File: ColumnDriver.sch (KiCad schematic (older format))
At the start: 7 parts

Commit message: Assigned footprints, add buffer capacitor, change description texts
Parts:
- added C?: 1uF, Capacitors_SMD:C_0805, symbol C_Small
- C1: renamed from C?; value C_Small -> 100nF; footprint (none) -> Capacitors_SMD:C_0603
- J1, J3: renamed from J?; footprint (none) -> Pin_Headers:Pin_Header_Straight_1x05_Pitch2.54mm
- J2: renamed from J?; footprint (none) -> Pin_Headers:Pin_Header_Straight_1x02_Pitch2.54mm
- J4: renamed from J?; footprint (none) -> Pin_Headers:Pin_Header_Straight_1x16_Pitch2.54mm
- U1: renamed from U?; value 74HC595 -> 74HCT595; footprint (none) -> Housings_SOIC:SOIC-16_3.9x9.9mm_Pitch1.27mm
- U2: renamed from U?; footprint (none) -> Housings_SOIC:SOIC-18W_7.5x11.6mm_Pitch1.27mm
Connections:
- net GND: now also U1.13 (G), C?.2
- net VCC: now also C?.1
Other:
- note added: "+5V0"
- note added: "Decoupling / Buffer"
- note added: "Inductors"
- note added: "Output"
- note removed: "+3V3 - +5V0"
- note removed: "Decoupling"
- moved on the sheet: C1
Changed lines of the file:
@@
 $EndDescr
 $Comp
-L 74HC595 U?
+L 74HC595 U1
 U 1 1 59204501
 P 4850 3200
-F 0 "U?" H 5000 3800 50  0000 C CNN
-F 1 "74HC595" H 4850 2600 50  0000 C CNN
-F 2 "" H 4850 3200 50  0001 C CNN
+F 0 "U1" H 5000 3800 50  0000 C CNN
+F 1 "74HCT595" H 4850 2600 50  0000 C CNN
+F 2 "Housings_SOIC:SOIC-16_3.9x9.9mm_Pitch1.27mm" H 4850 3200 50  0001 C CNN
 F 3 "" H 4850 3200 50  0001 C CNN
 	1    4850 3200
@@
 $EndComp
 $Comp
-L CONN_01X05 J?
+L CONN_01X05 J1
 U 1 1 59204744
 P 850 2050
-F 0 "J?" H 850 2350 50  0000 C CNN
+F 0 "J1" H 850 2350 50  0000 C CNN
 F 1 "CONN_01X05" V 950 2050 50  0000 C CNN
-F 2 "" H 850 2050 50  0001 C CNN
+F 2 "Pin_Headers:Pin_Header_Straight_1x05_Pitch2.54mm" H 850 2050 50  0001 C CNN
 F 3 "" H 850 2050 50  0001 C CNN
 	1    850  2050
@@
 $EndComp
 $Comp
-L CONN_01X05 J?
+L CONN_01X05 J3
 U 1 1 592048A3
 P 10700 1950
-F 0 "J?" H 10700 2250 50  0000 C CNN
+F 0 "J3" H 10700 2250 50  0000 C CNN
 F 1 "CONN_01X05" V 10800 1950 50  0000 C CNN
-F 2 "" H 10700 1950 50  0001 C CNN
+F 2 "Pin_Headers:Pin_Header_Straight_1x05_Pitch2.54mm" H 10700 1950 50  0001 C CNN
 F 3 "" H 10700 1950 50  0001 C CNN
 	1    10700 1950
@@
 DOUT
 $Comp
-L GND #PWR?
+L GND #PWR6
 U 1 1 59204A7B
 P 1300 1950
-F 0 "#PWR?" H 1300 1700 50  0001 C CNN
+F 0 "#PWR6" H 1300 1700 50  0001 C CNN
 F 1 "GND" H 1300 1800 50  0000 C CNN
 F 2 "" H 1300 1950 50  0001 C CNN
@@
 DOUT
 $Comp
-L VCC #PWR?
+L VCC #PWR3
 U 1 1 59204C65
 P 1150 1800
-F 0 "#PWR?" H 1150 1650 50  0001 C CNN
+F 0 "#PWR3" H 1150 1650 50  0001 C CNN
 F 1 "VCC" H 1150 1950 50  0000 C CNN
 F 2 "" H 1150 1800 50  0001 C CNN
@@
 $EndComp
 $Comp
-L GND #PWR?
+L GND #PWR2
 U 1 1 59204D53
-P 900 7450
-F 0 "#PWR?" H 900 7200 50  0001 C CNN
-F 1 "GND" H 900 7300 50  0000 C CNN
-F 2 "" H 900 7450 50  0001 C CNN
-F 3 "" H 900 7450 50  0001 C CNN
-	1    900  7450
-	1    0    0    -1
-$EndComp
-$Comp
-L VCC #PWR?
+P 1350 7450
+F 0 "#PWR2" H 1350 7200 50  0001 C CNN
+F 1 "GND" H 1350 7300 50  0000 C CNN
+F 2 "" H 1350 7450 50  0001 C CNN
+F 3 "" H 1350 7450 50  0001 C CNN
+	1    1350 7450
+	1    0    0    -1
+$EndComp
+$Comp
+L VCC #PWR1
 U 1 1 59204E34
-P 900 7050
-F 0 "#PWR?" H 900 6900 50  0001 C CNN
-F 1 "VCC" H 900 7200 50  0000 C CNN
-F 2 "" H 900 7050 50  0001 C CNN
-F 3 "" H 900 7050 50  0001 C CNN
-	1    900  7050
-	1    0    0    -1
-$EndComp
-$Comp
-L C_Small C?
+P 1350 7050
+F 0 "#PWR1" H 1350 6900 50  0001 C CNN
+F 1 "VCC" H 1350 7200 50  0000 C CNN
+F 2 "" H 1350 7050 50  0001 C CNN
+F 3 "" H 1350 7050 50  0001 C CNN
+	1    1350 7050
+	1    0    0    -1
+$EndComp
+$Comp
+L C_Small C1
 U 1 1 59204EED
-P 900 7250
-F 0 "C?" H 910 7320 50  0000 L CNN
-F 1 "C_Small" H 910 7170 50  0000 L CNN
-F 2 "" H 900 7250 50  0001 C CNN
-F 3 "" H 900 7250 50  0001 C CNN
-	1    900  7250
-	1    0    0    -1
-$EndComp
-$Comp
-L CONN_01X02 J?
+P 1350 7250
+F 0 "C1" H 1360 7320 50  0000 L CNN
+F 1 "100nF" H 1360 7170 50  0000 L CNN
+F 2 "Capacitors_SMD:C_0603" H 1350 7250 50  0001 C CNN
+F 3 "" H 1350 7250 50  0001 C CNN
+	1    1350 7250
+	1    0    0    -1
+$EndComp
+$Comp
+L CONN_01X02 J2
 U 1 1 5920547C
 P 900 850
-F 0 "J?" H 900 1000 50  0000 C CNN
+F 0 "J2" H 900 1000 50  0000 C CNN
 F 1 "CONN_01X02" V 1000 850 50  0000 C CNN
-F 2 "" H 900 850 50  0001 C CNN
+F 2 "Pin_Headers:Pin_Header_Straight_1x02_Pitch2.54mm" H 900 850 50  0001 C CNN
 F 3 "" H 900 850 50  0001 C CNN
 	1    900  850
@@
 $EndComp
 $Comp
-L GND #PWR?
+L GND #PWR5
 U 1 1 592054FB
 P 1200 950
-F 0 "#PWR?" H 1200 700 50  0001 C CNN
+F 0 "#PWR5" H 1200 700 50  0001 C CNN
 F 1 "GND" H 1200 800 50  0000 C CNN
 F 2 "" H 1200 950 50  0001 C CNN
@@
 $EndComp
 $Comp
-L VDD #PWR?
+L VDD #PWR4
 U 1 1 59205580
 P 1200 750
-F 0 "#PWR?" H 1200 600 50  0001 C CNN
+F 0 "#PWR4" H 1200 600 50  0001 C CNN
 F 1 "VDD" H 1200 900 50  0000 C CNN
 F 2 "" H 1200 750 50  0001 C CNN
@@
 	1    0    0    -1
 $EndComp
-Text Notes 550  600  0    60   ~ 0
+Text Notes 700  600  0    60   ~ 0
 +7V0
-Text Notes 550  1550 0    60   ~ 0
-+3V3 - +5V0
-$Comp
-L VDD #PWR?
+Text Notes 650  1700 0    60   ~ 0
++5V0
+$Comp
+L VDD #PWR9
 U 1 1 59205882
 P 6900 3550
-F 0 "#PWR?" H 6900 3400 50  0001 C CNN
+F 0 "#PWR9" H 6900 3400 50  0001 C CNN
 F 1 "VDD" H 6900 3700 50  0000 C CNN
 F 2 "" H 6900 3550 50  0001 C CNN
@@
 $EndComp
 $Comp
-L GND #PWR?
+L GND #PWR8
 U 1 1 592058D5
 P 6450 3850
-F 0 "#PWR?" H 6450 3600 50  0001 C CNN
+F 0 "#PWR8" H 6450 3600 50  0001 C CNN
 F 1 "GND" H 6450 3700 50  0000 C CNN
 F 2 "" H 6450 3850 50  0001 C CNN
@@
 	1    0    0    -1
 $EndComp
-Text Notes 550  1400 0    60   ~ 0
+Text Notes 650  1550 0    60   ~ 0
 Input
-Text Notes 550  6700 0    60   ~ 0
-Decoupling
-$Comp
-L CONN_01X16 J?
+Text Notes 650  6800 0    60   ~ 0
+Decoupling / Buffer
+$Comp
+L CONN_01X16 J4
 U 1 1 59205A9C
 P 10700 3400
-F 0 "J?" H 10700 4250 50  0000 C CNN
+F 0 "J4" H 10700 4250 50  0000 C CNN
 F 1 "CONN_01X16" V 10800 3400 50  0000 C CNN
-F 2 "" H 10700 3400 50  0001 C CNN
+F 2 "Pin_Headers:Pin_Header_Straight_1x16_Pitch2.54mm" H 10700 3400 50  0001 C CNN
 F 3 "" H 10700 3400 50  0001 C CNN
 	1    10700 3400
@@
 $EndComp
 $Comp
-L VDD #PWR?
+L VDD #PWR11
 U 1 1 59205AFC
 P 10350 2600
-F 0 "#PWR?" H 10350 2450 50  0001 C CNN
+F 0 "#PWR11" H 10350 2450 50  0001 C CNN
 F 1 "VDD" H 10350 2750 50  0000 C CNN
 F 2 "" H 10350 2600 50  0001 C CNN
@@
 DOT_6
 $Comp
-L ULN2803A U?
+L ULN2803A U2
 U 1 1 5920634D
 P 6450 3050
-F 0 "U?" H 6450 3575 50  0000 C CNN
+F 0 "U2" H 6450 3575 50  0000 C CNN
 F 1 "ULN2803A" H 6450 3500 50  0000 C CNN
-F 2 "" H 6500 2400 50  0001 L CNN
+F 2 "Housings_SOIC:SOIC-18W_7.5x11.6mm_Pitch1.27mm" H 6500 2400 50  0001 L CNN
 F 3 "" H 6550 2950 50  0001 C CNN
 	1    6450 3050
@@
 DOT_7
 $Comp
-L VCC #PWR?
+L VCC #PWR12
 U 1 1 59206E49
 P 10400 1700
-F 0 "#PWR?" H 10400 1550 50  0001 C CNN
+F 0 "#PWR12" H 10400 1550 50  0001 C CNN
 F 1 "VCC" H 10400 1850 50  0000 C CNN
 F 2 "" H 10400 1700 50  0001 C CNN
@@
 $EndComp
 $Comp
-L GND #PWR?
+L GND #PWR10
 U 1 1 59206E70
 P 10200 1850
-F 0 "#PWR?" H 10200 1600 50  0001 C CNN
+F 0 "#PWR10" H 10200 1600 50  0001 C CNN
 F 1 "GND" H 10200 1700 50  0000 C CNN
 F 2 "" H 10200 1850 50  0001 C CNN
@@
 	1150 1850 1150 1800
 Wire Wire Line
-	900  7150 900  7050
-Wire Wire Line
-	900  7350 900  7450
+	1350 7150 1350 7050
+Wire Wire Line
+	1350 7350 1350 7450
 Wire Wire Line
 	4150 2750 3950 2750
@@
 Wire Wire Line
 	10500 2050 10250 2050
+$Comp
+L GND #PWR7
+U 1 1 592167C3
+P 4050 3450
+F 0 "#PWR7" H 4050 3200 50  0001 C CNN
+F 1 "GND" H 4050 3300 50  0000 C CNN
+F 2 "" H 4050 3450 50  0001 C CNN
+F 3 "" H 4050 3450 50  0001 C CNN
+	1    4050 3450
+	1    0    0    -1
+$EndComp
+Wire Wire Line
+	4150 3350 4050 3350
+Wire Wire Line
+	4050 3350 4050 3450
+Text Notes 10300 2400 0    60   ~ 0
+Inductors
+Text Notes 10350 1500 0    60   ~ 0
+Output
+$Comp
+L C_Small C?
+U 1 1 59216FCE
+P 900 7250
+F 0 "C?" H 910 7320 50  0000 L CNN
+F 1 "1uF" H 910 7170 50  0000 L CNN
+F 2 "Capacitors_SMD:C_0805" H 900 7250 50  0001 C CNN
+F 3 "" H 900 7250 50  0001 C CNN
+	1    900  7250
+	1    0    0    -1
+$EndComp
+$Comp
+L VCC #PWR?
+U 1 1 5921706D
+P 900 7050
+F 0 "#PWR?" H 900 6900 50  0001 C CNN
+F 1 "VCC" H 900 7200 50  0000 C CNN
+F 2 "" H 900 7050 50  0001 C CNN
+F 3 "" H 900 7050 50  0001 C CNN
+	1    900  7050
+	1    0    0    -1
+$EndComp
+$Comp
+L GND #PWR?
+U 1 1 59217090
+P 900 7450
+F 0 "#PWR?" H 900 7200 50  0001 C CNN
+F 1 "GND" H 900 7300 50  0000 C CNN
+F 2 "" H 900 7450 50  0001 C CNN
+F 3 "" H 900 7450 50  0001 C CNN
+	1    900  7450
+	1    0    0    -1
+$EndComp
+Wire Wire Line
+	900  7050 900  7150
+Wire Wire Line
+	900  7350 900  7450
 $EndSCHEMATC

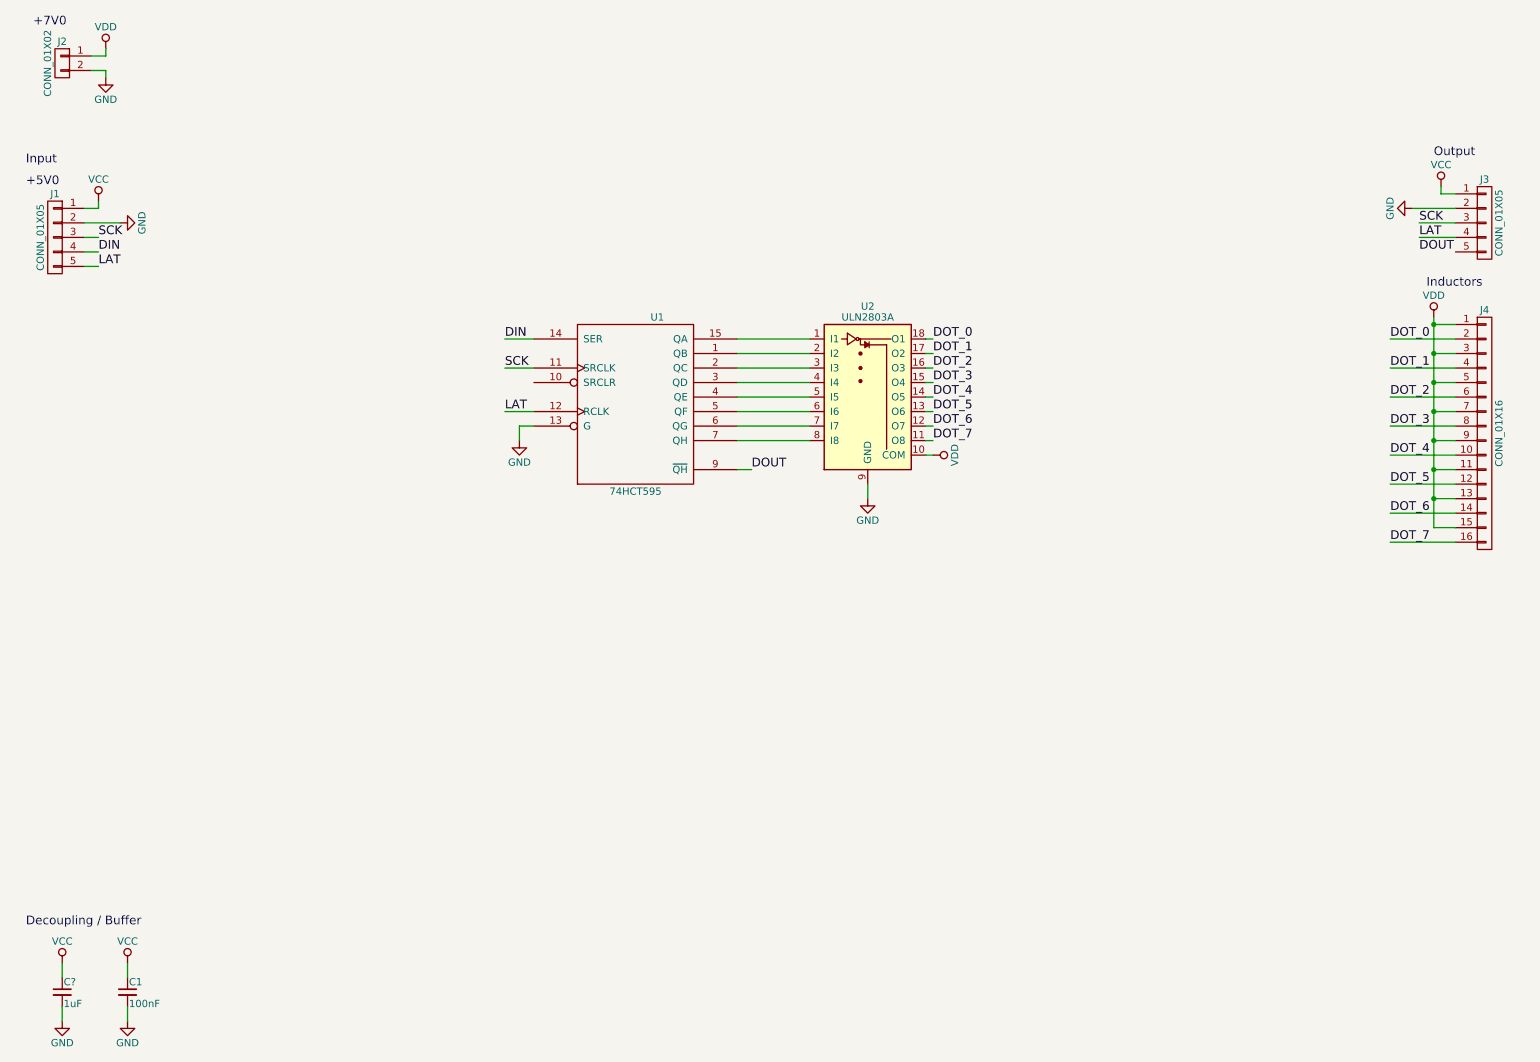
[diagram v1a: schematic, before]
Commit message: First Layout, incl. schematic adaption, 16x smd pads instead of one connector 1x16
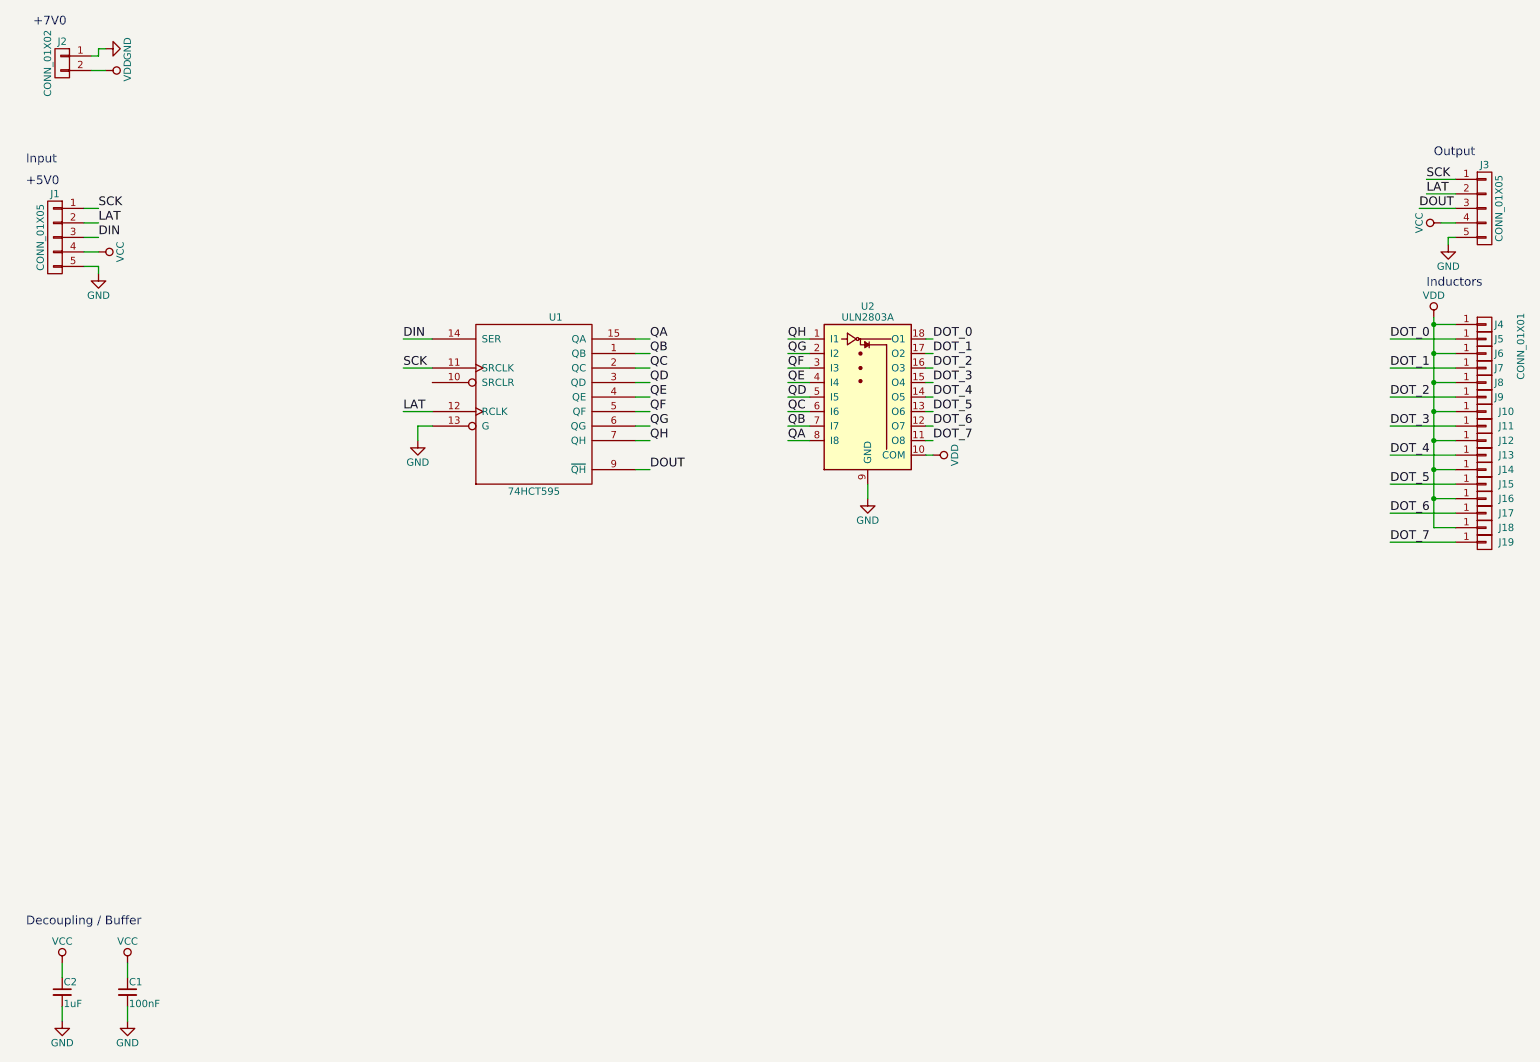
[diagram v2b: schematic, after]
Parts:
- removed J4: CONN_01X16, Pin_Headers:Pin_Header_Straight_1x16_Pitch2.54mm, symbol CONN_01X16
- added J10, J11, J12, J13, J14, J15, J16, J17, J18, J19, J4, J5, J6, J7, J8, J9: CONN_01X01, KiCadLib:1Pin_1x3mm, symbol CONN_01X01
- gave numbers to parts that had none: 1
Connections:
- net DIN: now also J1.3 (P3); no longer J1.4 (P4)
- net DOT_0: now also J5.1 (P1)
- net DOT_1: now also J7.1 (P1)
- net DOT_2: now also J9.1 (P1)
- net DOT_3: now also J11.1 (P1)
- net DOT_4: now also J13.1 (P1)
- net DOT_5: now also J15.1 (P1)
- net DOT_6: now also J17.1 (P1)
- net DOT_7: now also J19.1 (P1)
- net DOUT: now also J3.3 (P3)
- net GND: now also J1.5 (P5), J2.1 (P1), J3.5 (P5); no longer J1.2 (P2), J2.2 (P2), J3.2 (P2)
- net LAT: now also J1.2 (P2), J3.2 (P2); no longer J1.5 (P5), J3.4 (P4)
- net SCK: now also J1.1 (P1), J3.1 (P1); no longer J1.3 (P3), J3.3 (P3)
- net VCC: now also J1.4 (P4), J3.4 (P4); no longer J1.1 (P1), J3.1 (P1)
- net VDD: now also J2.2 (P2), J10.1 (P1), J12.1 (P1), J14.1 (P1), J16.1 (P1), J18.1 (P1), J4.1 (P1), J6.1 (P1), J8.1 (P1); no longer J2.1 (P1)
- net QB: now reaches U1.1 (QB)
- net QB: now also U2.7 (I7); no longer U2.2 (I2)
- net QA: now reaches U1.15 (QA)
- net QA: now also U2.8 (I8); no longer U2.1 (I1)
- net QC: now reaches U1.2 (QC)
- net QC: now also U2.6 (I6); no longer U2.3 (I3)
- net QD: now reaches U1.3 (QD)
- net QD: now also U2.5 (I5); no longer U2.4 (I4)
- net QE: now reaches U1.4 (QE)
- net QE: now also U2.4 (I4); no longer U2.5 (I5)
- net QF: now reaches U1.5 (QF)
- net QF: now also U2.3 (I3); no longer U2.6 (I6)
- net QG: now reaches U1.6 (QG)
- net QG: now also U2.2 (I2); no longer U2.7 (I7)
- net QH: now reaches U1.7 (QH)
- net QH: now also U2.1 (I1); no longer U2.8 (I8)
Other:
- moved on the sheet: J3, U1
